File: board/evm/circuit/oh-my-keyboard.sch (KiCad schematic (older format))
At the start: 0 parts

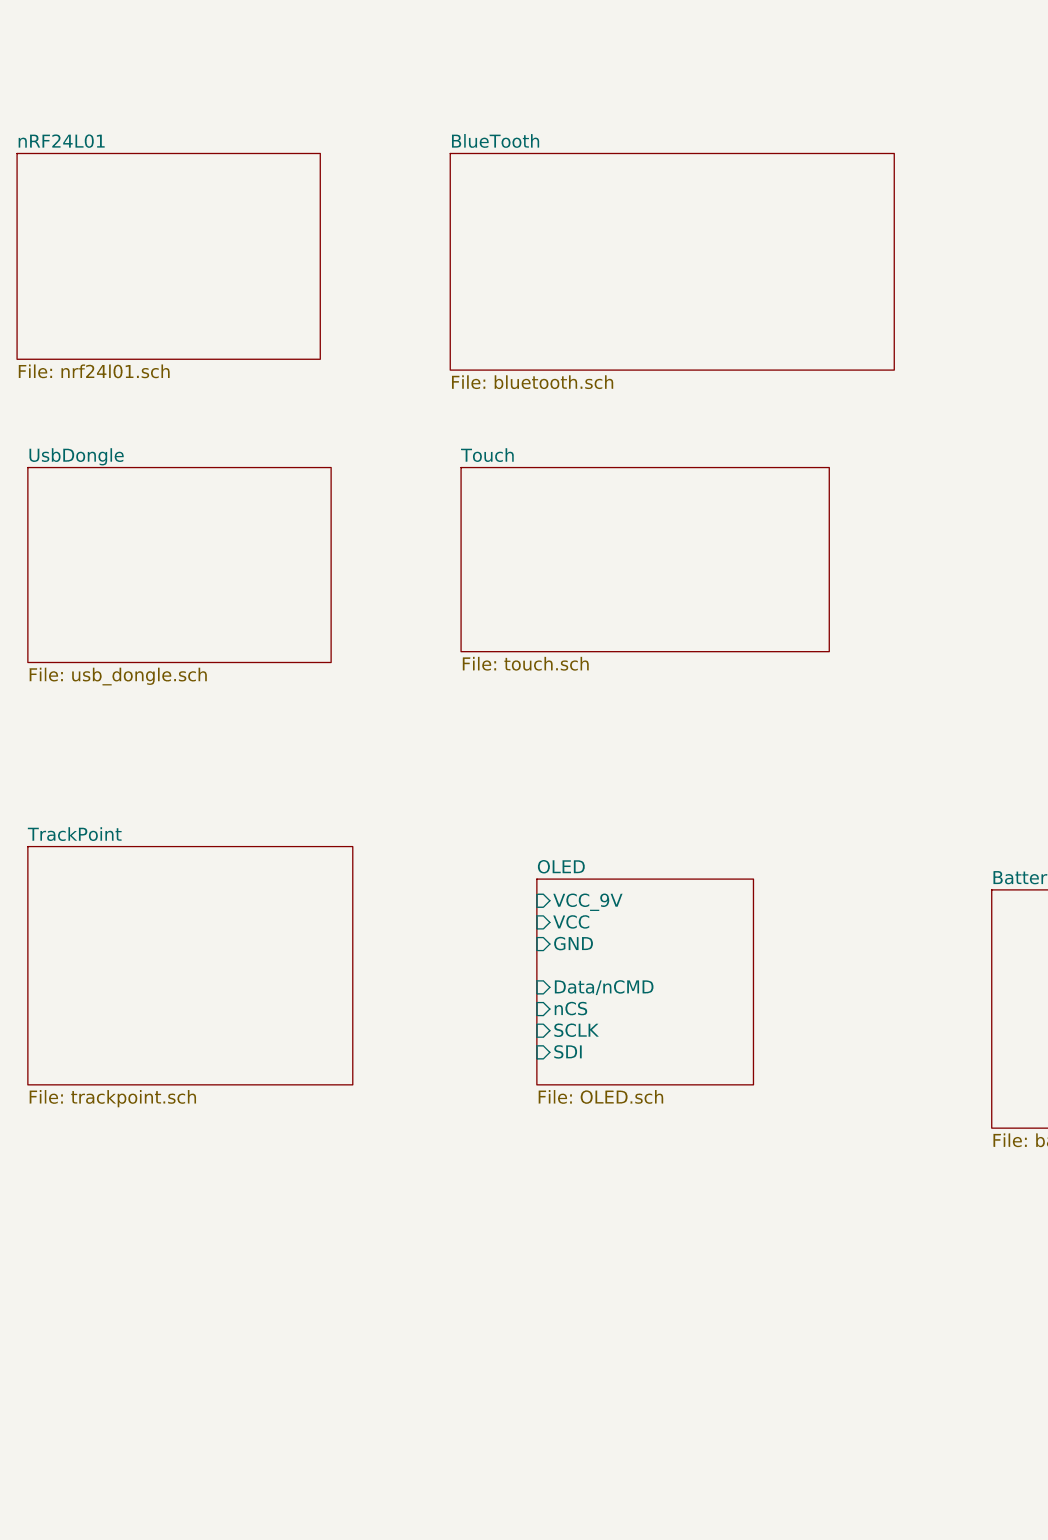
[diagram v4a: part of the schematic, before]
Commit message: still working for sch
All done except for battery, which need more consideration on scheme of
QC2.0 (or QC3.0?), bidirectional charge.
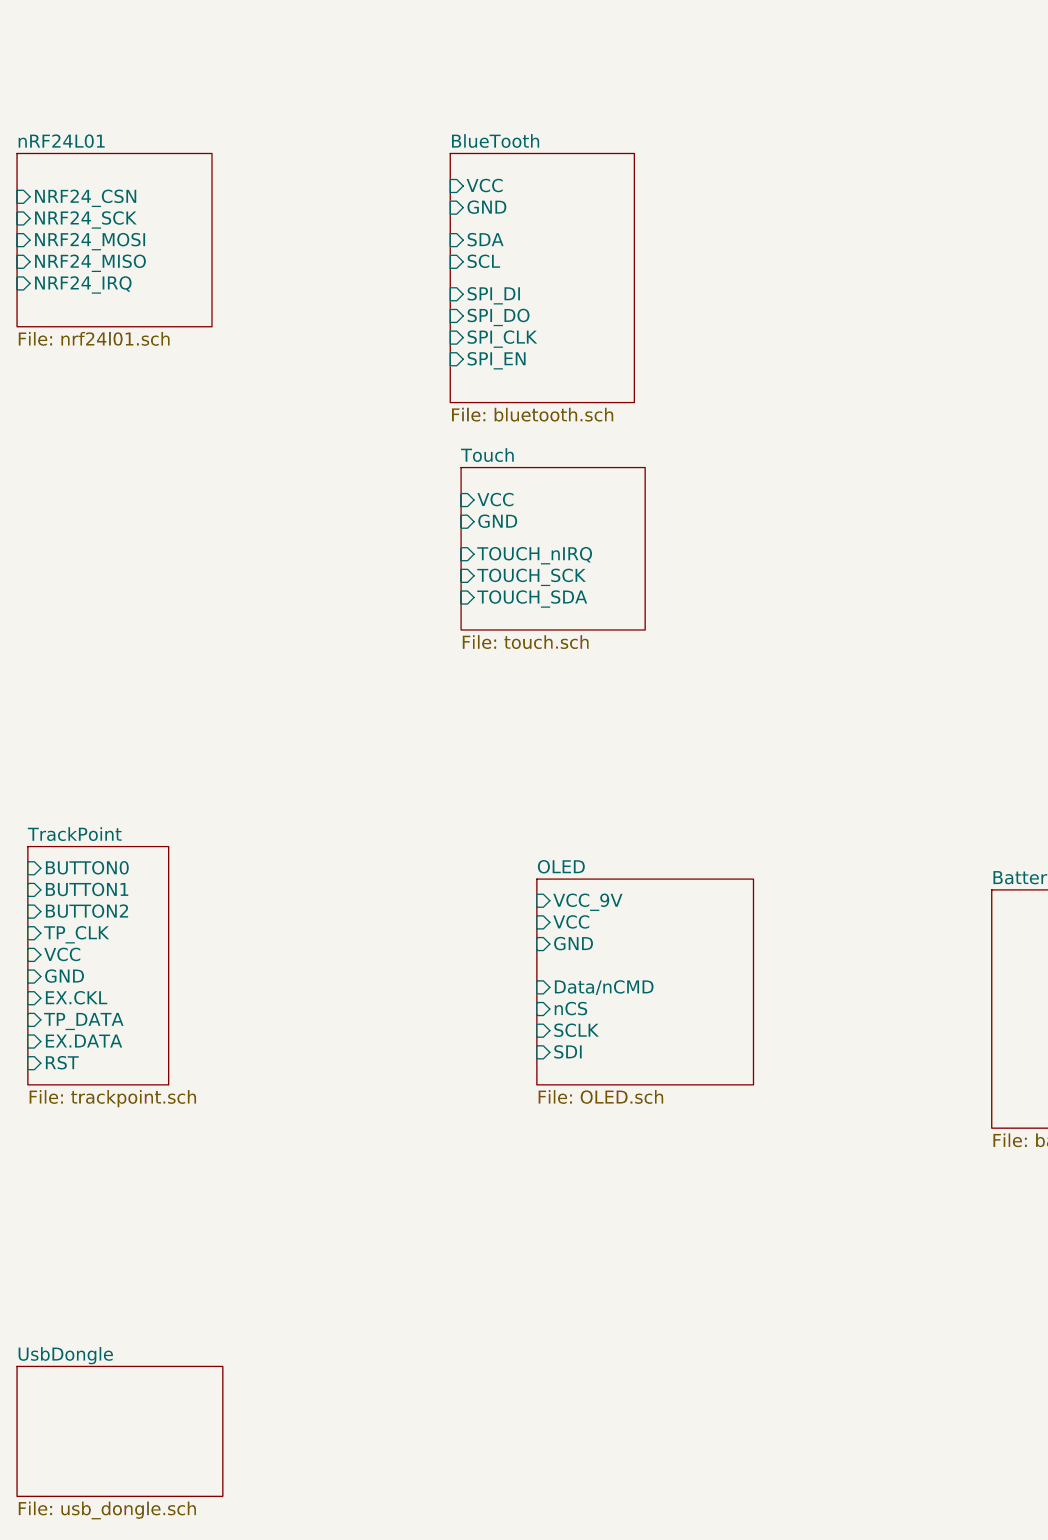
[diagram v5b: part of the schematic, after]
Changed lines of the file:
@@
 LIBS:contrib
 LIBS:valves
-LIBS:stm8
-LIBS:stm32
-LIBS:74xgxx
-LIBS:ac-dc
-LIBS:actel
 LIBS:Altera
-LIBS:analog_devices
-LIBS:battery_management
-LIBS:bbd
-LIBS:brooktre
-LIBS:cmos_ieee
-LIBS:dc-dc
-LIBS:diode
-LIBS:elec-unifil
-LIBS:ESD_Protection
-LIBS:ftdi
-LIBS:gennum
-LIBS:graphic
-LIBS:hc11
-LIBS:ir
-LIBS:Lattice
-LIBS:logo
-LIBS:maxim
-LIBS:microchip_dspic33dsc
-LIBS:microchip_pic10mcu
-LIBS:microchip_pic12mcu
-LIBS:microchip_pic16mcu
-LIBS:microchip_pic18mcu
-LIBS:microchip_pic32mcu
-LIBS:motor_drivers
-LIBS:msp430
-LIBS:nordicsemi
-LIBS:nxp_armmcu
-LIBS:onsemi
-LIBS:Oscillators
-LIBS:powerint
-LIBS:Power_Management
-LIBS:pspice
-LIBS:references
-LIBS:relays
-LIBS:rfcom
-LIBS:sensors
-LIBS:silabs
-LIBS:supertex
-LIBS:switches
-LIBS:transf
-LIBS:ttl_ieee
-LIBS:video
-LIBS:Worldsemi
-LIBS:Xicor
-LIBS:Zilog
 LIBS:my_kicad
 LIBS:oh-my-keyboard-cache
@@
 $EndSheet
 $Sheet
-S 2100 3300 1400 950
+S 2100 3300 900  800
 U 57545D59
 F0 "nRF24L01" 60
 F1 "nrf24l01.sch" 60
-$EndSheet
-$Sheet
-S 4100 3300 2050 1000
+F2 "NRF24_CSN" I L 2100 3500 60
+F3 "NRF24_SCK" I L 2100 3600 60
+F4 "NRF24_MOSI" I L 2100 3700 60
+F5 "NRF24_MISO" I L 2100 3800 60
+F6 "NRF24_IRQ" I L 2100 3900 60
+$EndSheet
+$Sheet
+S 4100 3300 850  1150
 U 57545D83
 F0 "BlueTooth" 60
 F1 "bluetooth.sch" 60
-$EndSheet
-$Sheet
-S 2150 4750 1400 900
+F2 "VCC" I L 4100 3450 60
+F3 "GND" I L 4100 3550 60
+F4 "SDA" I L 4100 3700 60
+F5 "SCL" I L 4100 3800 60
+F6 "SPI_DI" I L 4100 3950 60
+F7 "SPI_DO" I L 4100 4050 60
+F8 "SPI_CLK" I L 4100 4150 60
+F9 "SPI_EN" I L 4100 4250 60
+$EndSheet
+$Sheet
+S 2100 8900 950  600
 U 5754760F
 F0 "UsbDongle" 60
@@
 $EndSheet
 $Sheet
-S 4150 4750 1700 850
+S 4150 4750 850  750
 U 57549417
 F0 "Touch" 60
 F1 "touch.sch" 60
-$EndSheet
-$Sheet
-S 2150 6500 1500 1100
+F2 "TOUCH_nIRQ" I L 4150 5150 60
+F3 "TOUCH_SCK" I L 4150 5250 60
+F4 "TOUCH_SDA" I L 4150 5350 60
+F5 "VCC" I L 4150 4900 60
+F6 "GND" I L 4150 5000 60
+$EndSheet
+$Sheet
+S 2150 6500 650  1100
 U 57593E70
 F0 "TrackPoint" 60
 F1 "trackpoint.sch" 60
-$EndSheet
-$Sheet
+F2 "BUTTON2" I L 2150 6800 60
+F3 "BUTTON1" I L 2150 6700 60
+F4 "BUTTON0" I L 2150 6600 60
+F5 "TP_CLK" I L 2150 6900 60
+F6 "VCC" I L 2150 7000 60
+F7 "GND" I L 2150 7100 60
+F8 "EX.CKL" I L 2150 7200 60
+F9 "TP_DATA" I L 2150 7300 60
+F10 "EX.DATA" I L 2150 7400 60
+F11 "RST" I L 2150 7500 60
+$EndSheet
+$Sheet

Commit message: battery sch nearly done
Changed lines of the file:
@@
 LIBS:contrib
 LIBS:valves
+LIBS:stm8
+LIBS:stm32
+LIBS:74xgxx
+LIBS:ac-dc
+LIBS:actel
 LIBS:Altera
+LIBS:analog_devices
+LIBS:battery_management
+LIBS:bbd
+LIBS:brooktre
+LIBS:cmos_ieee
+LIBS:dc-dc
+LIBS:diode
+LIBS:elec-unifil
+LIBS:ESD_Protection
+LIBS:ftdi
+LIBS:gennum
+LIBS:graphic
+LIBS:hc11
+LIBS:ir
+LIBS:Lattice
+LIBS:logo
+LIBS:maxim
+LIBS:microchip_dspic33dsc
+LIBS:microchip_pic10mcu
+LIBS:microchip_pic12mcu
+LIBS:microchip_pic16mcu
+LIBS:microchip_pic18mcu
+LIBS:microchip_pic32mcu
+LIBS:motor_drivers
+LIBS:msp430
+LIBS:nordicsemi
+LIBS:nxp_armmcu
+LIBS:onsemi
+LIBS:Oscillators
+LIBS:powerint
+LIBS:Power_Management
+LIBS:pspice
+LIBS:references
+LIBS:relays
+LIBS:rfcom
+LIBS:sensors
+LIBS:silabs
+LIBS:supertex
+LIBS:switches
+LIBS:transf
+LIBS:ttl_ieee
+LIBS:video
+LIBS:Worldsemi
+LIBS:Xicor
+LIBS:Zilog
 LIBS:my_kicad
 LIBS:oh-my-keyboard-cache
@@
 F0 "OLED" 60
 F1 "OLED.sch" 60
-F2 "VCC_9V" I L 4500 6750 60
 F3 "GND" I L 4500 6950 60
 F4 "VCC" I L 4500 6850 60

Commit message: working on leak current detection
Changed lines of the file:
@@
 LIBS:contrib
 LIBS:valves
-LIBS:stm8
-LIBS:stm32
-LIBS:74xgxx
-LIBS:ac-dc
-LIBS:actel
 LIBS:Altera
-LIBS:analog_devices
-LIBS:battery_management
-LIBS:bbd
-LIBS:brooktre
-LIBS:cmos_ieee
-LIBS:dc-dc
-LIBS:diode
-LIBS:elec-unifil
-LIBS:ESD_Protection
-LIBS:ftdi
-LIBS:gennum
-LIBS:graphic
-LIBS:hc11
-LIBS:ir
-LIBS:Lattice
-LIBS:logo
-LIBS:maxim
-LIBS:microchip_dspic33dsc
-LIBS:microchip_pic10mcu
-LIBS:microchip_pic12mcu
-LIBS:microchip_pic16mcu
-LIBS:microchip_pic18mcu
-LIBS:microchip_pic32mcu
-LIBS:motor_drivers
-LIBS:msp430
-LIBS:nordicsemi
-LIBS:nxp_armmcu
-LIBS:onsemi
-LIBS:Oscillators
-LIBS:powerint
-LIBS:Power_Management
-LIBS:pspice
-LIBS:references
-LIBS:relays
-LIBS:rfcom
-LIBS:sensors
-LIBS:silabs
-LIBS:supertex
-LIBS:switches
-LIBS:transf
-LIBS:ttl_ieee
-LIBS:video
-LIBS:Worldsemi
-LIBS:Xicor
-LIBS:Zilog
 LIBS:my_kicad
 LIBS:oh-my-keyboard-cache
@@
 $EndDescr
 $Sheet
-S 7350 3200 700  2400
+S 6200 2250 850  2300
 U 57532E7B
 F0 "MCU" 60
 F1 "mcu.sch" 60
-F2 "VCC" I L 7350 3300 60
-F3 "GND" I L 7350 3450 60
-F4 "VCC_5V" I L 7350 3600 60
-F5 "D0" I L 7350 3850 60
-F6 "D1" I L 7350 3950 60
-F7 "D2" I L 7350 4050 60
-F8 "D3" I L 7350 4150 60
-F9 "D4" I L 7350 4250 60
-F10 "D5" I L 7350 4350 60
-F11 "D6" I L 7350 4450 60
-F12 "D7" I L 7350 4550 60
-F13 "D8" I L 7350 4650 60
-F14 "D9" I L 7350 4750 60
-F15 "D10" I L 7350 4850 60
-F16 "D11" I L 7350 4950 60
-F17 "D12" I L 7350 5050 60
-F18 "D13" I L 7350 5150 60
-F19 "D14" I L 7350 5250 60
-F20 "D15" I L 7350 5350 60
-F21 "A16" I R 8050 3850 60
-F22 "A17" I R 8050 3950 60
-F23 "A18" I R 8050 4050 60
-F24 "A19" I R 8050 4150 60
-F25 "A20" I R 8050 4250 60
-F26 "A21" I R 8050 4350 60
-F27 "A22" I R 8050 4450 60
-F28 "A23" I R 8050 4550 60
-F29 "nOE" I R 8050 4700 60
-F30 "nCS" I R 8050 4800 60
-F31 "nWE" I R 8050 4900 60
-$EndSheet
-$Sheet
-S 7450 1200 1400 1400
+F2 "VCC" I L 6200 2350 60
+F3 "GND" I L 6200 2450 60
+F4 "D0" I L 6200 2900 60
+F5 "D1" I L 6200 3000 60
+F6 "D2" I L 6200 3100 60
+F7 "D3" I L 6200 3200 60
+F8 "D4" I L 6200 3300 60
+F9 "D5" I L 6200 3400 60
+F10 "D6" I L 6200 3500 60
+F11 "D7" I L 6200 3600 60
+F12 "D8" I L 6200 3700 60
+F13 "D9" I L 6200 3800 60
+F14 "D10" I L 6200 3900 60
+F15 "D11" I L 6200 4000 60
+F16 "D12" I L 6200 4100 60
+F17 "D13" I L 6200 4200 60
+F18 "D14" I L 6200 4300 60
+F19 "D15" I L 6200 4400 60
+F20 "A16" I R 7050 2900 60
+F21 "A17" I R 7050 3000 60
+F22 "A18" I R 7050 3100 60
+F23 "A19" I R 7050 3200 60
+F24 "A20" I R 7050 3300 60
+F25 "A21" I R 7050 3400 60
+F26 "A22" I R 7050 3500 60
+F27 "A23" I R 7050 3600 60
+F28 "nOE" I R 7050 3750 60
+F29 "nCS" I R 7050 3850 60
+F30 "nWE" I R 7050 3950 60
+F31 "Device_D+" I L 6200 2600 60
+F32 "Device_D-" I L 6200 2700 60
+F33 "Host_D+" I R 7050 2350 60
+F34 "Host_D-" I R 7050 2450 60
+$EndSheet
+$Sheet
+S 1950 850  1400 1400
 U 57532E7E
 F0 "baseboard" 60
 F1 "baseboard.sch" 60
-F2 "VCC" I L 7450 1350 60
-F3 "GND" I L 7450 1450 60
-F4 "KEY_serial_in" I L 7450 1550 60
-F5 "KEY_nPL" I L 7450 1650 60
-F6 "KEY_CLK" I L 7450 1750 60
-F7 "KEY_nCE" I L 7450 1850 60
-F8 "KEY_serial_out" I R 8850 1350 60
-F9 "LED_Shift_CLK" I L 7450 2050 60
-F10 "LED_serial_in" I L 7450 2150 60
-F11 "LED_nCLR" I L 7450 2250 60
-F12 "LED_Storage_CLK" I L 7450 2350 60
-F13 "LED_nOE" I L 7450 2450 60
-F14 "LED_serial_out" I R 8850 1450 60
+F2 "VCC" I L 1950 1000 60
+F3 "GND" I L 1950 1100 60
+F4 "KEY_serial_in" I L 1950 1200 60
+F5 "KEY_nPL" I L 1950 1300 60
+F6 "KEY_CLK" I L 1950 1400 60
+F7 "KEY_nCE" I L 1950 1500 60
+F8 "KEY_serial_out" I R 3350 1000 60
+F9 "LED_Shift_CLK" I L 1950 1700 60
+F10 "LED_serial_in" I L 1950 1800 60
+F11 "LED_nCLR" I L 1950 1900 60
+F12 "LED_Storage_CLK" I L 1950 2000 60
+F13 "LED_nOE" I L 1950 2100 60
+F14 "LED_serial_out" I R 3350 1100 60
 $EndSheet
 $Sheet
@@
 $EndSheet
 $Sheet
-S 4100 3300 850  1150
+S 2200 4650 850  1150
 U 57545D83
 F0 "BlueTooth" 60
 F1 "bluetooth.sch" 60
-F2 "VCC" I L 4100 3450 60
-F3 "GND" I L 4100 3550 60
-F4 "SDA" I L 4100 3700 60
-F5 "SCL" I L 4100 3800 60
-F6 "SPI_DI" I L 4100 3950 60
-F7 "SPI_DO" I L 4100 4050 60
-F8 "SPI_CLK" I L 4100 4150 60
-F9 "SPI_EN" I L 4100 4250 60
+F2 "VCC" I L 2200 4800 60
+F3 "GND" I L 2200 4900 60
+F4 "SDA" I L 2200 5050 60
+F5 "SCL" I L 2200 5150 60
+F6 "SPI_DI" I L 2200 5300 60
+F7 "SPI_DO" I L 2200 5400 60
+F8 "SPI_CLK" I L 2200 5500 60
+F9 "SPI_EN" I L 2200 5600 60
 $EndSheet
 $Sheet
@@
 F6 "SCLK" I L 4500 7350 60
 F7 "SDI" I L 4500 7450 60
-$EndSheet
-$Sheet
-S 6600 6700 1600 1100
+F8 "VCC_12V" I L 4500 6750 60
+$EndSheet
+$Sheet
+S 6450 6600 1200 1950
 U 57594611
 F0 "Battery" 60
 F1 "battery.sch" 60
+F2 "BatteryBoost_EN" I L 6450 7800 60
+F3 "BAT_SCL" I L 6450 7350 60
+F4 "BAT_SDA" I L 6450 7450 60
+F5 "BAT_INT" I L 6450 7550 60
+F6 "BAT_nCE" I L 6450 7150 60
+F7 "BAT_DSEL" I L 6450 7250 60
+F8 "Device_D+" I L 6450 8050 60
+F9 "Device_D-" I L 6450 8150 60
+F10 "Host_D-" I L 6450 8400 60
+F11 "Host_D+" I L 6450 8300 60
+F12 "ChargeOutputEN" I L 6450 7900 60
+F13 "12V" I L 6450 6700 60
+F14 "3.3V" I L 6450 6900 60
+F15 "GND" I L 6450 7000 60
+F16 "BAT_OTG_EN" I L 6450 7700 60
+F17 "5V" I L 6450 6800 60
 $EndSheet
 $EndSCHEMATC
